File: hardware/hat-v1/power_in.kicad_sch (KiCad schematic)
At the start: 27 parts, among them J1 BATT pads, Q1 CSD19537Q3, Q2 BSS138, Q6 BSS138, U1 TPS26631RGER, U2 INA226AIDGSR

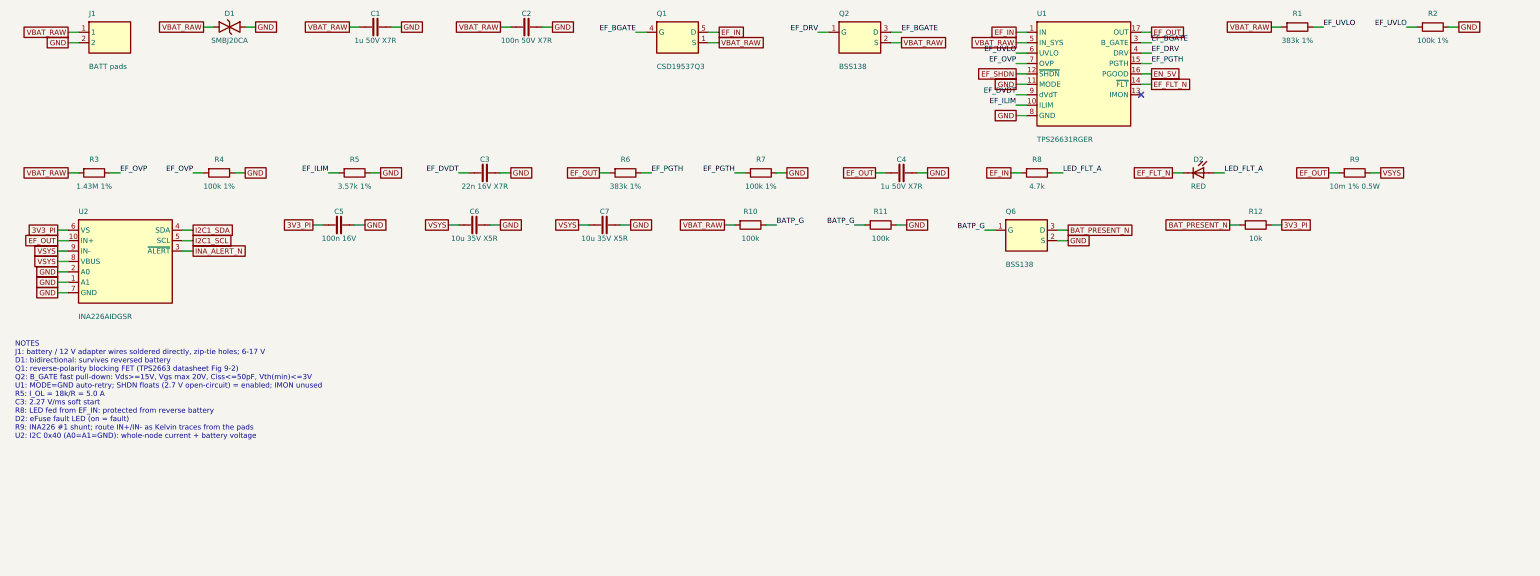
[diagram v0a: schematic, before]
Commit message: HAT v1 schematic: apply adversarial review (power + digital/security/DFM)
AUTO-ON above buck EN window, BENCH no longer blocks power-off, OVP moved
to 19.2 V with input damper, Tier A parts DNP for JLC, debug links
removable for production, antenna short limited, stock footprints where
available, cap ratings/DC-bias fixes, CONSOLE_TX/RX naming.

Co-Authored-By: Claude Opus 5.5 <noreply@anthropic.com>
Claude-Session: https://claude.ai/code/session_01MLRuxTEmuMV82xcNLE62jW
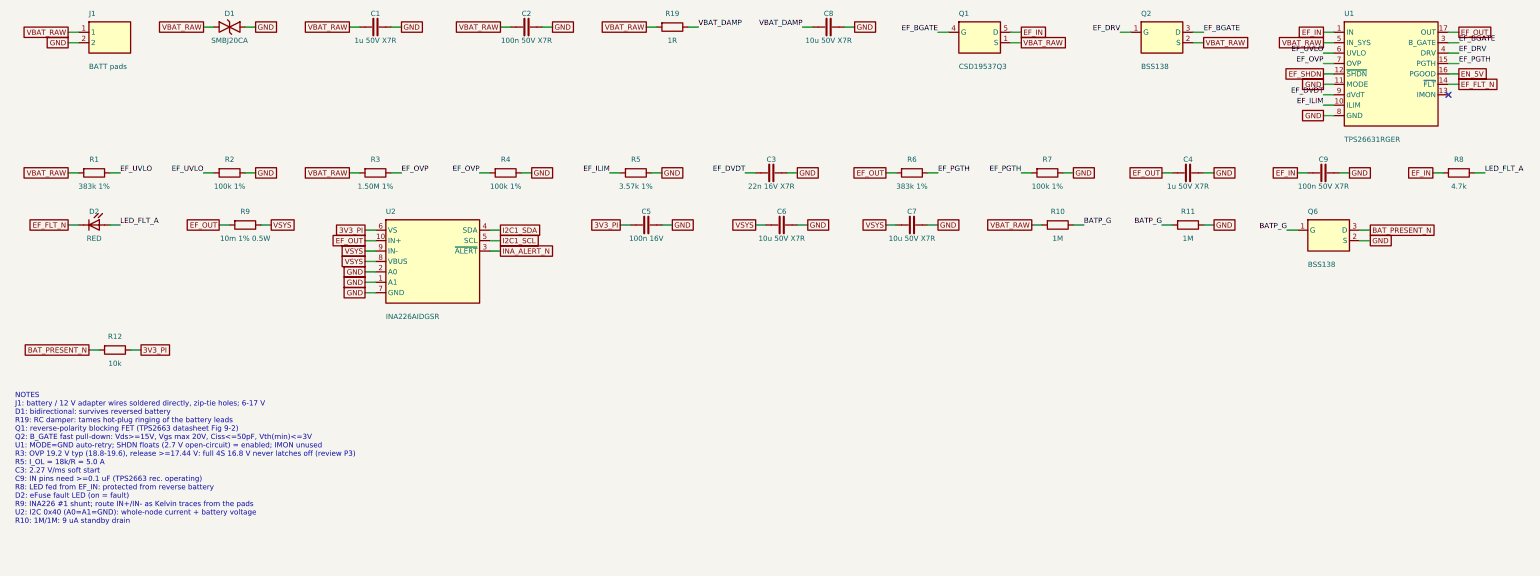
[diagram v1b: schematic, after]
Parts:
- added C8: 10u 50V X7R, Capacitor_SMD:C_1210_3225Metric, symbol batman:C
- added C9: 100n 50V X7R, Capacitor_SMD:C_0402_1005Metric, symbol batman:C
- added R19: 1R, Resistor_SMD:R_0805_2012Metric, symbol batman:R
- C6, C7: value 10u 35V X5R -> 10u 50V X7R; footprint Capacitor_SMD:C_1206_3216Metric -> Capacitor_SMD:C_1210_3225Metric
- D2: footprint LED_SMD:LED_0603_1608Metric -> LED_SMD:LED_0402_1005Metric
- J1: now left out of the parts list
- Q1: footprint batman:TI_VSON-CLIP-8_3.3x3.3mm -> Package_SON:VSON-8_3.3x3.3mm_P0.65mm_NexFET
- R10: value 100k -> 1M; Note (none) -> 1M/1M: 9 uA standby drain
- R11: value 100k -> 1M
- R3: value 1.43M 1% -> 1.50M 1%; Note (none) -> OVP 19.2 V typ (18.8-19.6), release >=17.44 V: full 4S 16.8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
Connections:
- net GND: now also C8.2, C9.2
- net IN: now also C9.1; no longer Q1.6 (D), Q1.7 (D), Q1.8 (D), Q1.9 (D)
- net VBAT_RAW: now also R19.1
- new net VBAT_DAMP: C8.1, R19.2
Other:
- note added: "NOTES J1: battery / 12 V adapter wires soldered directly, zip-tie holes; 6-17 V D1: bidirectional: survives reversed battery R19: RC damper: tames hot-plug ringing of the battery leads Q1: reverse-polarity blocking FET (TPS2663 datasheet Fig 9-2) Q2: B_GATE fast pull-down: Vds>=15V, Vgs max 20V, Ciss<=50pF, Vth(min)<=3V U1: MODE=GND auto-retry; SHDN floats (2.7 V open-circuit) = enabled; IMON unu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"
- note removed: "NOTES J1: battery / 12 V adapter wires soldered directly, zip-tie holes; 6-17 V D1: bidirectional: survives reversed battery Q1: reverse-polarity blocking FET (TPS2663 datasheet Fig 9-2) Q2: B_GATE fast pull-down: Vds>=15V, Vgs max 20V, Ciss<=50pF, Vth(min)<=3V U1: MODE=GND auto-retry; SHDN floats (2.7 V open-circuit) = enabled; IMON unused R5: I_OL = 18k/R = 5.0 A C3: 2.27 V/ms soft start R8: LE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"
- moved on the sheet: C3, C4, C5, C6, C7, D2, Q1, Q2, Q6, R1, R10, R11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

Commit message: HAT v1: pre-fab simulations (ngspice + behavioural sequencing), damper 0.47R + 2x10uF
S1 hot-plug ringing, S2 HaLow rail pi-filter under TX bursts, S3 eight
power-sequencing scenarios, S4 Monte Carlo of a slowly recovering battery
(0/400 stuck-off vs 274/400 with the pre-review AUTO-ON divider).

Co-Authored-By: Claude Opus 5.5 <noreply@anthropic.com>
Claude-Session: https://claude.ai/code/session_01MLRuxTEmuMV82xcNLE62jW
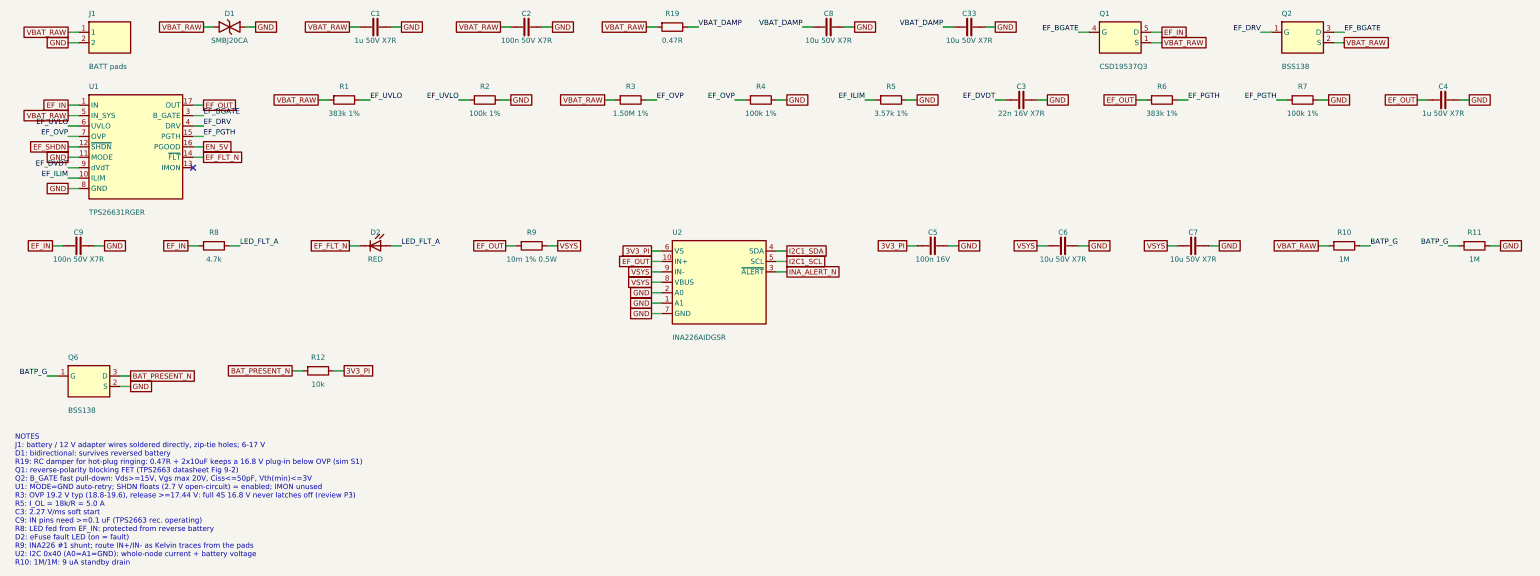
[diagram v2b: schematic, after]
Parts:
- added C33: 10u 50V X7R, Capacitor_SMD:C_1210_3225Metric, symbol batman:C
- R19: value 1R -> 0.47R; Note RC damper: tames hot-plug ringing of the battery leads -> RC damper for hot-plug ringing: 0.47R + 2x10uF keeps a 16.8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
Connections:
- net GND: now also C33.2
- net VBAT_DAMP: now also C33.1
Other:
- note added: "NOTES J1: battery / 12 V adapter wires soldered directly, zip-tie holes; 6-17 V D1: bidirectional: survives reversed battery R19: RC damper for hot-plug ringing: 0.47R + 2x10uF keeps a 16.8 V plug-in below OVP (sim S1) Q1: reverse-polarity blocking FET (TPS2663 datasheet Fig 9-2) Q2: B_GATE fast pull-down: Vds>=15V, Vgs max 20V, Ciss<=50pF, Vth(min)<=3V U1: MODE=GND auto-retry; SHDN floats (2.7 V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"
- note removed: "NOTES J1: battery / 12 V adapter wires soldered directly, zip-tie holes; 6-17 V D1: bidirectional: survives reversed battery R19: RC damper: tames hot-plug ringing of the battery leads Q1: reverse-polarity blocking FET (TPS2663 datasheet Fig 9-2) Q2: B_GATE fast pull-down: Vds>=15V, Vgs max 20V, Ciss<=50pF, Vth(min)<=3V U1: MODE=GND auto-retry; SHDN floats (2.7 V open-circuit) = enabled; IMON unu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"
- moved on the sheet: C3, C4, C5, C6, C7, C9, D2, Q1, Q2, Q6, R1, R10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

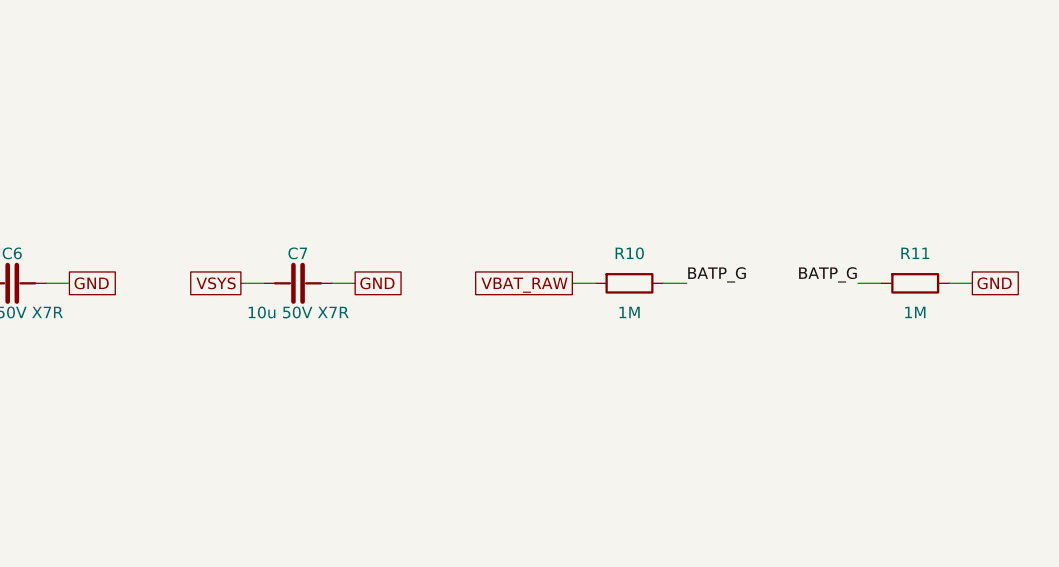
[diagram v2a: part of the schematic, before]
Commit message: HAT v1: hand placement of the power path (5V buck at the header, battery bottom-left), routing pipeline
layout.py: anchors for ~45 power/IC parts, proximity placement for the rest,
net classes, In1 GND plane (Specctra power layer), DSN export, Freerouting,
SES import, power-track widening, GND pours, DRC. SW1 and C7 removed
(user decision / space). Wi-Fi keep-out reduced to an L shape so header
pins 1-4 stay routable.

Co-Authored-By: Claude Opus 5.5 <noreply@anthropic.com>
Claude-Session: https://claude.ai/code/session_01MLRuxTEmuMV82xcNLE62jW
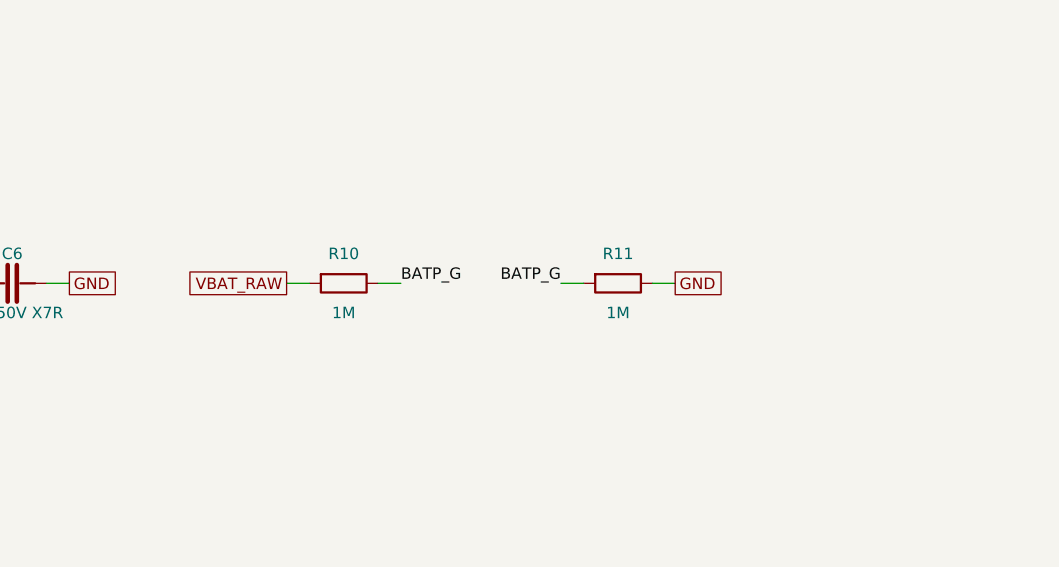
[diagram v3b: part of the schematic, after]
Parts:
- removed C7: 10u 50V X7R, Capacitor_SMD:C_1210_3225Metric, symbol batman:C
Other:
- moved on the sheet: R10, R11
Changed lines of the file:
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@@
   (global_label "GND" (shape passive) (at 276.86 80.01 0) (fields_autoplaced) (effects (font (size 1.27 1.27)) (justify left))
     (property "Intersheetrefs" "${INTERSHEET_REFS}" (at 276.86 80.01 0) (effects (font (size 1.27 1.27)) hide)))
-  (symbol (lib_id "batman:C") (at 302.26 80.01 0) (unit 1) (in_bom yes) (on_board yes) (dnp no)
-    (property "Reference" "C7" (at 302.26 77.47 0) (effects (font (size 1.27 1.27)) (justify bottom)))
-    (property "Value" "10u 50V X7R" (at 302.26 82.55 0) (effects (font (size 1.27 1.27)) (justify top)))
-    (property "Footprint" "Capacitor_SMD:C_1210_3225Metric" (at 302.26 80.01 0) (effects (font (size 1.27 1.27)) hide))
-    (property "Datasheet" "" (at 302.26 80.01 0) (effects (font (size 1.27 1.27)) hide))
-    (property "MPN" "" (at 302.26 80.01 0) (effects (font (size 1.27 1.27)) hide))
-    (property "Manufacturer" "" (at 302.26 80.01 0) (effects (font (size 1.27 1.27)) hide))
-    (property "Tier" "C" (at 302.26 80.01 0) (effects (font (size 1.27 1.27)) hide))
-    (property "LCSC" "" (at 302.26 80.01 0) (effects (font (size 1.27 1.27)) hide))
-    (property "Note" "" (at 302.26 80.01 0) (effects (font (size 1.27 1.27)) hide))
-    (pin "1")
-    (pin "2")
-    (instances (project "batman-hat" (path "/bad0bf22-4662-5834-886f-55d01014b15a/1adc0704-a6af-5b3a-93b0-790b7d9f73c9" (reference "C7") (unit 1))))
-  )
-  (wire (pts (xy 298.45 80.01) (xy 295.91 80.01)) (stroke (width 0) (type default)))
-  (global_label "VSYS" (shape passive) (at 295.91 80.01 180) (fields_autoplaced) (effects (font (size 1.27 1.27)) (justify right))
-    (property "Intersheetrefs" "${INTERSHEET_REFS}" (at 295.91 80.01 0) (effects (font (size 1.27 1.27)) hide)))
-  (wire (pts (xy 306.07 80.01) (xy 308.61 80.01)) (stroke (width 0) (type default)))
-  (global_label "GND" (shape passive) (at 308.61 80.01 0) (fields_autoplaced) (effects (font (size 1.27 1.27)) (justify left))
-    (property "Intersheetrefs" "${INTERSHEET_REFS}" (at 308.61 80.01 0) (effects (font (size 1.27 1.27)) hide)))
-  (symbol (lib_id "batman:R") (at 339.09 80.01 0) (unit 1) (in_bom yes) (on_board yes) (dnp no)
-    (property "Reference" "R10" (at 339.09 77.47 0) (effects (font (size 1.27 1.27)) (justify bottom)))
-    (property "Value" "1M" (at 339.09 82.55 0) (effects (font (size 1.27 1.27)) (justify top)))
-    (property "Footprint" "Resistor_SMD:R_0402_1005Metric" (at 339.09 80.01 0) (effects (font (size 1.27 1.27)) hide))
-    (property "Datasheet" "" (at 339.09 80.01 0) (effects (font (size 1.27 1.27)) hide))
-    (property "MPN" "" (at 339.09 80.01 0) (effects (font (size 1.27 1.27)) hide))
-    (property "Manufacturer" "" (at 339.09 80.01 0) (effects (font (size 1.27 1.27)) hide))
-    (property "Tier" "C" (at 339.09 80.01 0) (effects (font (size 1.27 1.27)) hide))
-    (property "LCSC" "" (at 339.09 80.01 0) (effects (font (size 1.27 1.27)) hide))
-    (property "Note" "1M/1M: 9 uA standby drain" (at 339.09 80.01 0) (effects (font (size 1.27 1.27)) hide))
+  (symbol (lib_id "batman:R") (at 307.34 80.01 0) (unit 1) (in_bom yes) (on_board yes) (dnp no)
+    (property "Reference" "R10" (at 307.34 77.47 0) (effects (font (size 1.27 1.27)) (justify bottom)))
+    (property "Value" "1M" (at 307.34 82.55 0) (effects (font (size 1.27 1.27)) (justify top)))
+    (property "Footprint" "Resistor_SMD:R_0402_1005Metric" (at 307.34 80.01 0) (effects (font (size 1.27 1.27)) hide))
+    (property "Datasheet" "" (at 307.34 80.01 0) (effects (font (size 1.27 1.27)) hide))
+    (property "MPN" "" (at 307.34 80.01 0) (effects (font (size 1.27 1.27)) hide))
+    (property "Manufacturer" "" (at 307.34 80.01 0) (effects (font (size 1.27 1.27)) hide))
+    (property "Tier" "C" (at 307.34 80.01 0) (effects (font (size 1.27 1.27)) hide))
+    (property "LCSC" "" (at 307.34 80.01 0) (effects (font (size 1.27 1.27)) hide))
+    (property "Note" "1M/1M: 9 uA standby drain" (at 307.34 80.01 0) (effects (font (size 1.27 1.27)) hide))
     (pin "1")
     (pin "2")
     (instances (project "batman-hat" (path "/bad0bf22-4662-5834-886f-55d01014b15a/1adc0704-a6af-5b3a-93b0-790b7d9f73c9" (reference "R10") (unit 1))))
   )
-  (wire (pts (xy 335.28 80.01) (xy 332.74 80.01)) (stroke (width 0) (type default)))
-  (global_label "VBAT_RAW" (shape passive) (at 332.74 80.01 180) (fields_autoplaced) (effects (font (size 1.27 1.27)) (justify right))
-    (property "Intersheetrefs" "${INTERSHEET_REFS}" (at 332.74 80.01 0) (effects (font (size 1.27 1.27)) hide)))
-  (wire (pts (xy 342.9 80.01) (xy 345.44 80.01)) (stroke (width 0) (type default)))
-  (label "BATP_G" (at 345.44 80.01 0) (fields_autoplaced) (effects (font (size 1.27 1.27)) (justify left bottom)))
-  (symbol (lib_id "batman:R") (at 370.84 80.01 0) (unit 1) (in_bom yes) (on_board yes) (dnp no)
-    (property "Reference" "R11" (at 370.84 77.47 0) (effects (font (size 1.27 1.27)) (justify bottom)))
-    (property "Value" "1M" (at 370.84 82.55 0) (effects (font (size 1.27 1.27)) (justify top)))
-    (property "Footprint" "Resistor_SMD:R_0402_1005Metric" (at 370.84 80.01 0) (effects (font (size 1.27 1.27)) hide))
-    (property "Datasheet" "" (at 370.84 80.01 0) (effects (font (size 1.27 1.27)) hide))
-    (property "MPN" "" (at 370.84 80.01 0) (effects (font (size 1.27 1.27)) hide))
-    (property "Manufacturer" "" (at 370.84 80.01 0) (effects (font (size 1.27 1.27)) hide))
-    (property "Tier" "C" (at 370.84 80.01 0) (effects (font (size 1.27 1.27)) hide))
-    (property "LCSC" "" (at 370.84 80.01 0) (effects (font (size 1.27 1.27)) hide))
-    (property "Note" "" (at 370.84 80.01 0) (effects (font (size 1.27 1.27)) hide))
+  (wire (pts (xy 303.53 80.01) (xy 300.99 80.01)) (stroke (width 0) (type default)))
+  (global_label "VBAT_RAW" (shape passive) (at 300.99 80.01 180) (fields_autoplaced) (effects (font (size 1.27 1.27)) (justify right))
+    (property "Intersheetrefs" "${INTERSHEET_REFS}" (at 300.99 80.01 0) (effects (font (size 1.27 1.27)) hide)))
+  (wire (pts (xy 311.15 80.01) (xy 313.69 80.01)) (stroke (width 0) (type default)))
+  (label "BATP_G" (at 313.69 80.01 0) (fields_autoplaced) (effects (font (size 1.27 1.27)) (justify left bottom)))
+  (symbol (lib_id "batman:R") (at 337.82 80.01 0) (unit 1) (in_bom yes) (on_board yes) (dnp no)
+    (property "Reference" "R11" (at 337.82 77.47 0) (effects (font (size 1.27 1.27)) (justify bottom)))
+    (property "Value" "1M" (at 337.82 82.55 0) (effects (font (size 1.27 1.27)) (justify top)))
+    (property "Footprint" "Resistor_SMD:R_0402_1005Metric" (at 337.82 80.01 0) (effects (font (size 1.27 1.27)) hide))
+    (property "Datasheet" "" (at 337.82 80.01 0) (effects (font (size 1.27 1.27)) hide))
+    (property "MPN" "" (at 337.82 80.01 0) (effects (font (size 1.27 1.27)) hide))
+    (property "Manufacturer" "" (at 337.82 80.01 0) (effects (font (size 1.27 1.27)) hide))
+    (property "Tier" "C" (at 337.82 80.01 0) (effects (font (size 1.27 1.27)) hide))
+    (property "LCSC" "" (at 337.82 80.01 0) (effects (font (size 1.27 1.27)) hide))
+    (property "Note" "" (at 337.82 80.01 0) (effects (font (size 1.27 1.27)) hide))
     (pin "1")
     (pin "2")
     (instances (project "batman-hat" (path "/bad0bf22-4662-5834-886f-55d01014b15a/1adc0704-a6af-5b3a-93b0-790b7d9f73c9" (reference "R11") (unit 1))))
   )
-  (wire (pts (xy 367.03 80.01) (xy 364.49 80.01)) (stroke (width 0) (type default)))
-  (label "BATP_G" (at 364.49 80.01 180) (fields_autoplaced) (effects (font (size 1.27 1.27)) (justify right bottom)))
-  (wire (pts (xy 374.65 80.01) (xy 377.19 80.01)) (stroke (width 0) (type default)))
-  (global_label "GND" (shape passive) (at 377.19 80.01 0) (fields_autoplaced) (effects (font (size 1.27 1.27)) (justify left))
-    (property "Intersheetrefs" "${INTERSHEET_REFS}" (at 377.19 80.01 0) (effects (font (size 1.27 1.27)) hide)))
+  (wire (pts (xy 334.01 80.01) (xy 331.47 80.01)) (stroke (width 0) (type default)))
+  (label "BATP_G" (at 331.47 80.01 180) (fields_autoplaced) (effects (font (size 1.27 1.27)) (justify right bottom)))
+  (wire (pts (xy 341.63 80.01) (xy 344.17 80.01)) (stroke (width 0) (type default)))
+  (global_label "GND" (shape passive) (at 344.17 80.01 0) (fields_autoplaced) (effects (font (size 1.27 1.27)) (justify left))
+    (property "Intersheetrefs" "${INTERSHEET_REFS}" (at 344.17 80.01 0) (effects (font (size 1.27 1.27)) hide)))
   (symbol (lib_id "batman:NMOS") (at 33.02 113.03 0) (unit 1) (in_bom yes) (on_board yes) (dnp no)
     (property "Reference" "Q6" (at 27.94 107.95 0) (effects (font (size 1.27 1.27)) (justify left bottom)))
